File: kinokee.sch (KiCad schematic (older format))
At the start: 14 parts

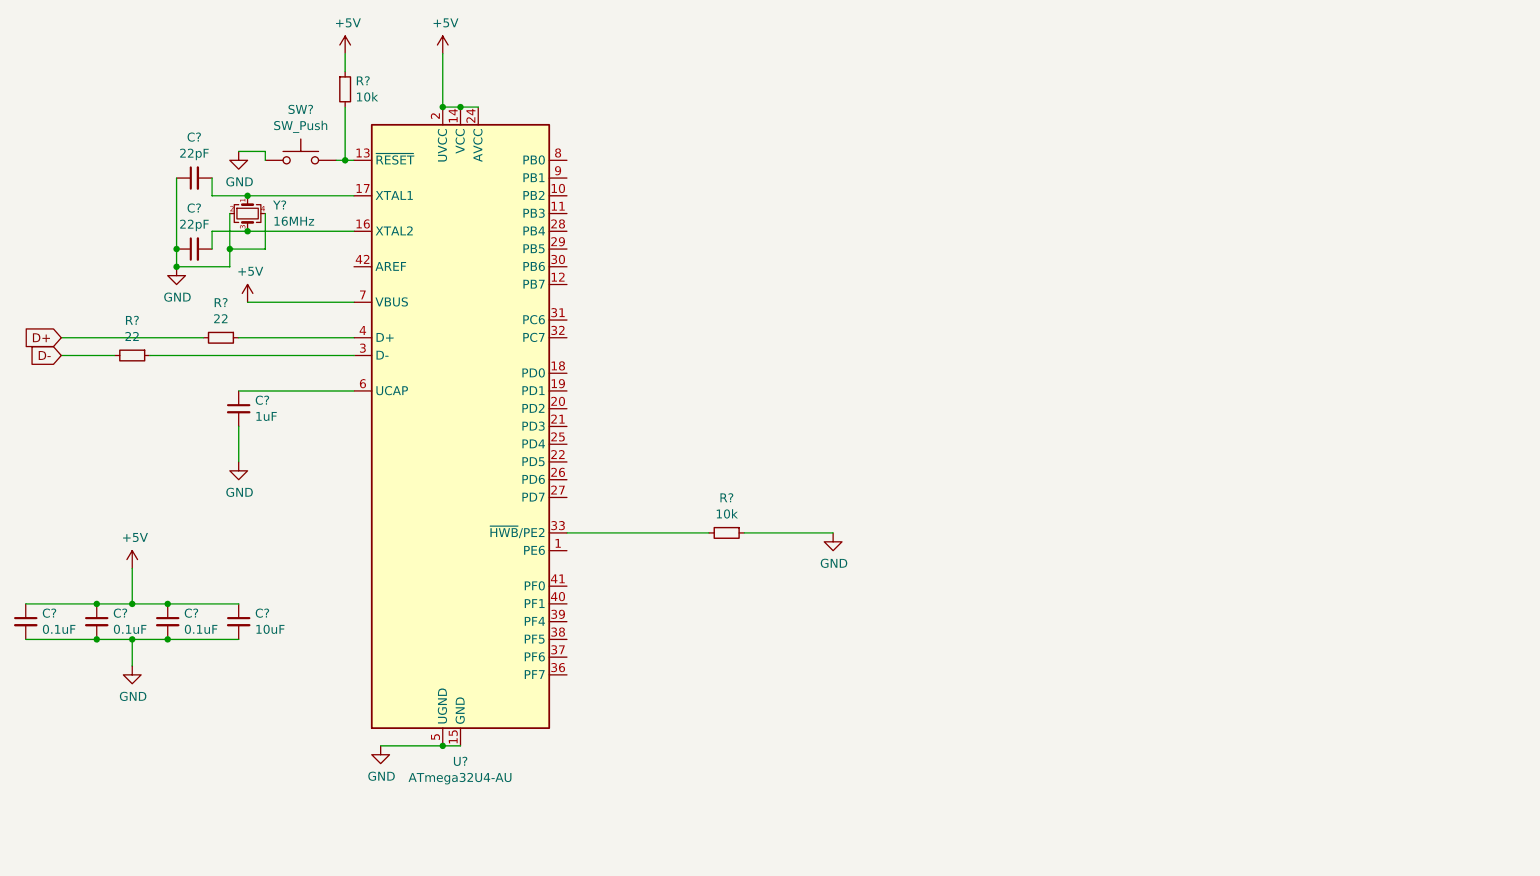
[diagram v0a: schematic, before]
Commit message: add 2x2 matrix and usb to schematic
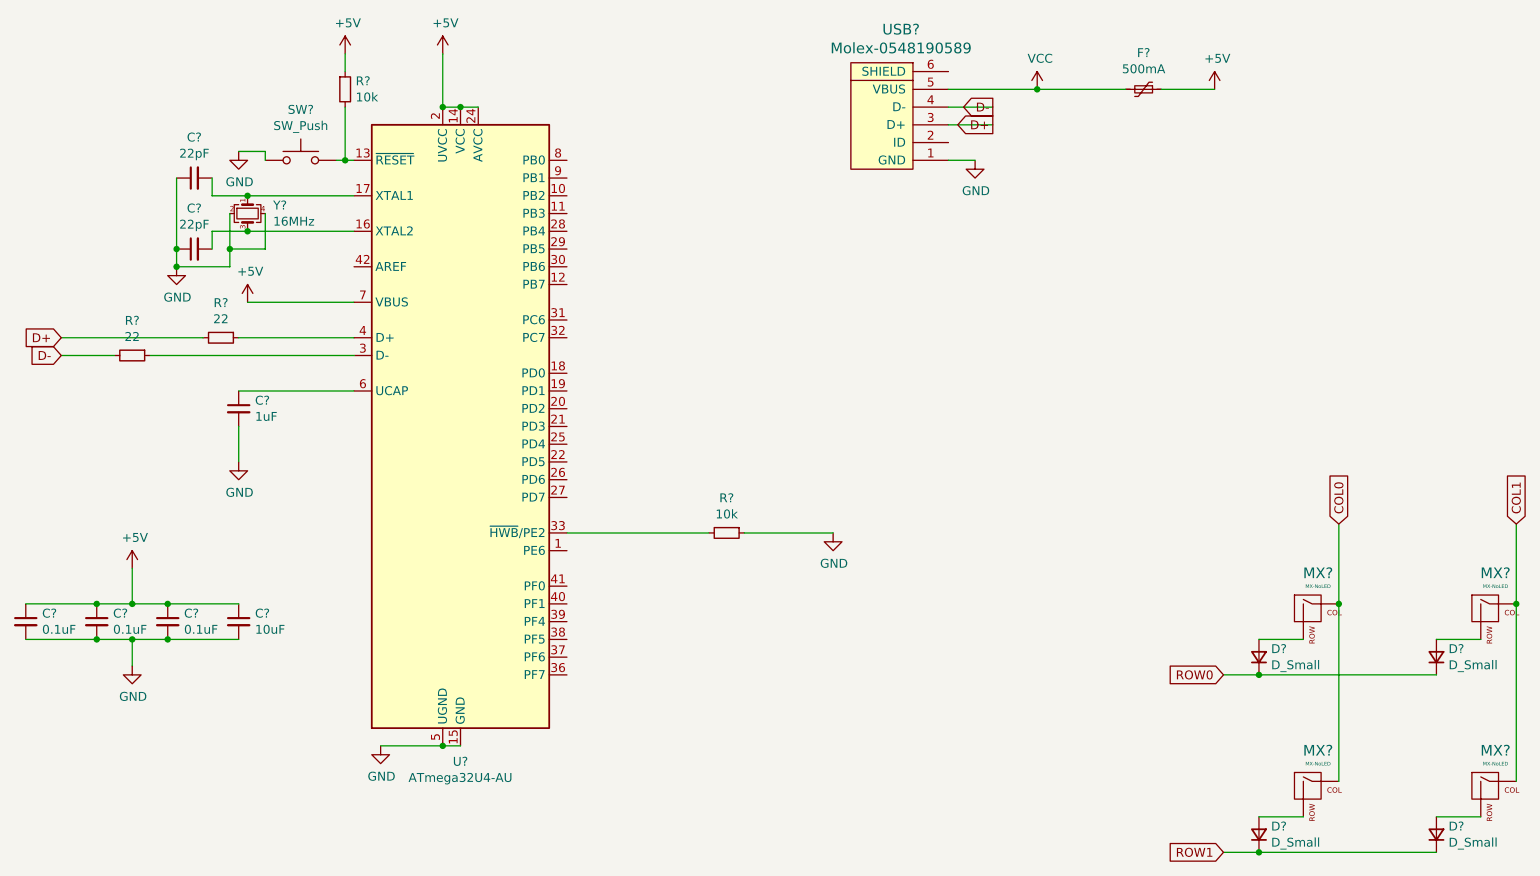
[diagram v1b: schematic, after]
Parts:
- added D? (x4): D_Small, symbol Device:D_Small
- added F?: 500mA, symbol Device:Polyfuse_Small
- added MX? (x4): MX-NoLED, symbol MX_Alps_Hybrid:MX-NoLED
- added USB?: Molex-0548190589, symbol random-keyboard-parts:Molex-0548190589
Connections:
- net +5V: now also F?.1
- net D+: now also USB?.3 (D+)
- net D-: now also USB?.4 (D-)
- net GND: now also USB?.1 (GND)
- new net: D?.2 (A), MX?.2 (ROW) (x4)
- new net COL0: MX?.1 (COL), MX?.1 (COL)
- new net COL1: MX?.1 (COL), MX?.1 (COL)
- new net ROW0: D?.1 (K), D?.1 (K)
- new net ROW1: D?.1 (K), D?.1 (K)
- new net VCC: F?.2, USB?.5 (VBUS)
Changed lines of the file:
@@
 EESchema Schematic File Version 4
+LIBS:kinokee-cache
 EELAYER 30 0
 EELAYER END
@@
 Text GLabel 1500 3100 0    50   Input ~ 0
 D-
+$Comp
+L random-keyboard-parts:Molex-0548190589 USB?
+U 1 1 61B5ADF8
+P 6200 1800
+F 0 "USB?" V 6737 1767 60  0000 C CNN
+F 1 "Molex-0548190589" V 6631 1767 60  0000 C CNN
+F 2 "" H 6200 1800 60  0001 C CNN
+F 3 "" H 6200 1800 60  0001 C CNN
+	1    6200 1800
+	0    -1   -1   0
+$EndComp
+$Comp
+L Device:Polyfuse_Small F?
+U 1 1 61B5F971
+P 7600 1600
+F 0 "F?" V 7395 1600 50  0000 C CNN
+F 1 "500mA" V 7486 1600 50  0000 C CNN
+F 2 "" H 7650 1400 50  0001 L CNN
+F 3 "~" H 7600 1600 50  0001 C CNN
+	1    7600 1600
+	0    1    1    0
+$EndComp
+$Comp
+L power:VCC #PWR?
+U 1 1 61B60F28
+P 7000 1600
+F 0 "#PWR?" H 7000 1450 50  0001 C CNN
+F 1 "VCC" H 7017 1773 50  0000 C CNN
+F 2 "" H 7000 1600 50  0001 C CNN
+F 3 "" H 7000 1600 50  0001 C CNN
+	1    7000 1600
+	1    0    0    -1
+$EndComp
+Wire Wire Line
+	6500 1600 7000 1600
+Wire Wire Line
+	7000 1600 7500 1600
+Connection ~ 7000 1600
+$Comp
+L power:+5V #PWR?
+U 1 1 61B6393F
+P 8000 1600
+F 0 "#PWR?" H 8000 1450 50  0001 C CNN
+F 1 "+5V" H 8015 1773 50  0000 C CNN
+F 2 "" H 8000 1600 50  0001 C CNN
+F 3 "" H 8000 1600 50  0001 C CNN
+	1    8000 1600
+	1    0    0    -1
+$EndComp
+Wire Wire Line
+	7700 1600 8000 1600
+Text GLabel 6750 1800 0    50   Output ~ 0
+D+
+Wire Wire Line
+	6500 1800 6750 1800
+Text GLabel 6750 1700 0    50   Output ~ 0
+D-
+Wire Wire Line
+	6500 1700 6750 1700
+$Comp
+L power:GND #PWR?
+U 1 1 61B68145
+P 6650 2000
+F 0 "#PWR?" H 6650 1750 50  0001 C CNN
+F 1 "GND" H 6655 1827 50  0000 C CNN
+F 2 "" H 6650 2000 50  0001 C CNN
+F 3 "" H 6650 2000 50  0001 C CNN
+	1    6650 2000
+	1    0    0    -1
+$EndComp
+Wire Wire Line
+	6500 2000 6650 2000
+$Comp
+L MX_Alps_Hybrid:MX-NoLED MX?
+U 1 1 61B6983E
+P 8550 4550
+F 0 "MX?" H 8583 4773 60  0000 C CNN
+F 1 "MX-NoLED" H 8583 4699 20  0000 C CNN
+F 2 "" H 7925 4525 60  0001 C CNN
+F 3 "" H 7925 4525 60  0001 C CNN
+	1    8550 4550
+	1    0    0    -1
+$EndComp
+$Comp
+L Device:D_Small D?
+U 1 1 61B6B0B0
+P 8250 4800
+F 0 "D?" V 8296 4732 50  0000 R CNN
+F 1 "D_Small" V 8205 4732 50  0000 R CNN
+F 2 "" V 8250 4800 50  0001 C CNN
+F 3 "~" V 8250 4800 50  0001 C CNN
+	1    8250 4800
+	0    -1   -1   0
+$EndComp
+Wire Wire Line
+	8250 4700 8500 4700
+$Comp
+L MX_Alps_Hybrid:MX-NoLED MX?
+U 1 1 61B6D2F5
+P 9550 4550
+F 0 "MX?" H 9583 4773 60  0000 C CNN
+F 1 "MX-NoLED" H 9583 4699 20  0000 C CNN
+F 2 "" H 8925 4525 60  0001 C CNN
+F 3 "" H 8925 4525 60  0001 C CNN
+	1    9550 4550
+	1    0    0    -1
+$EndComp
+$Comp
+L Device:D_Small D?
+U 1 1 61B6E845
+P 9250 4800
+F 0 "D?" V 9296 4732 50  0000 R CNN
+F 1 "D_Small" V 9205 4732 50  0000 R CNN
+F 2 "" V 9250 4800 50  0001 C CNN
+F 3 "~" V 9250 4800 50  0001 C CNN
+	1    9250 4800
+	0    -1   -1   0
+$EndComp
+$Comp
+L MX_Alps_Hybrid:MX-NoLED MX?
+U 1 1 61B7046B
+P 8550 5550
+F 0 "MX?" H 8583 5773 60  0000 C CNN
+F 1 "MX-NoLED" H 8583 5699 20  0000 C CNN
+F 2 "" H 7925 5525 60  0001 C CNN
+F 3 "" H 7925 5525 60  0001 C CNN
+	1    8550 5550
+	1    0    0    -1
+$EndComp
+$Comp
+L Device:D_Small D?
+U 1 1 61B70F93
+P 8250 5800
+F 0 "D?" V 8296 5732 50  0000 R CNN
+F 1 "D_Small" V 8205 5732 50  0000 R CNN
+F 2 "" V 8250 5800 50  0001 C CNN
+F 3 "~" V 8250 5800 50  0001 C CNN
+	1    8250 5800
+	0    -1   -1   0
+$EndComp
+$Comp
+L Device:D_Small D?
+U 1 1 61B71E0D
+P 9250 5800
+F 0 "D?" V 9296 5732 50  0000 R CNN
+F 1 "D_Small" V 9205 5732 50  0000 R CNN
+F 2 "" V 9250 5800 50  0001 C CNN
+F 3 "~" V 9250 5800 50  0001 C CNN
+	1    9250 5800
+	0    -1   -1   0
+$EndComp
+$Comp
+L MX_Alps_Hybrid:MX-NoLED MX?
+U 1 1 61B731E6
+P 9550 5550
+F 0 "MX?" H 9583 5773 60  0000 C CNN
+F 1 "MX-NoLED" H 9583 5699 20  0000 C CNN
+F 2 "" H 8925 5525 60  0001 C CNN
+F 3 "" H 8925 5525 60  0001 C CNN
+	1    9550 5550
+	1    0    0    -1
+$EndComp
+Wire Wire Line
+	8250 5700 8500 5700
+Wire Wire Line
+	9250 5700 9500 5700
+Wire Wire Line
+	9250 4700 9500 4700
+Wire Wire Line
+	8250 4900 9250 4900
+Wire Wire Line
+	8700 4500 8700 4050
+Wire Wire Line
+	9700 4500 9700 4050
+Wire Wire Line
+	9700 5500 9700 4500
+Connection ~ 9700 4500
+Wire Wire Line
+	9250 5900 8250 5900
+Wire Wire Line
+	8250 5900 8050 5900
+Connection ~ 8250 5900
+Wire Wire Line
+	8250 4900 8050 4900
+Connection ~ 8250 4900
+Wire Wire Line
+	8700 5500 8700 4500
+Connection ~ 8700 4500
+Text GLabel 8050 4900 0    50   Input ~ 0
+ROW0
+Text GLabel 8050 5900 0    50   Input ~ 0
+ROW1
+Text GLabel 8700 4050 1    50   Input ~ 0
+COL0
+Text GLabel 9700 4050 1    50   Input ~ 0
+COL1
 $EndSCHEMATC

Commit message: assign footprints to schematic
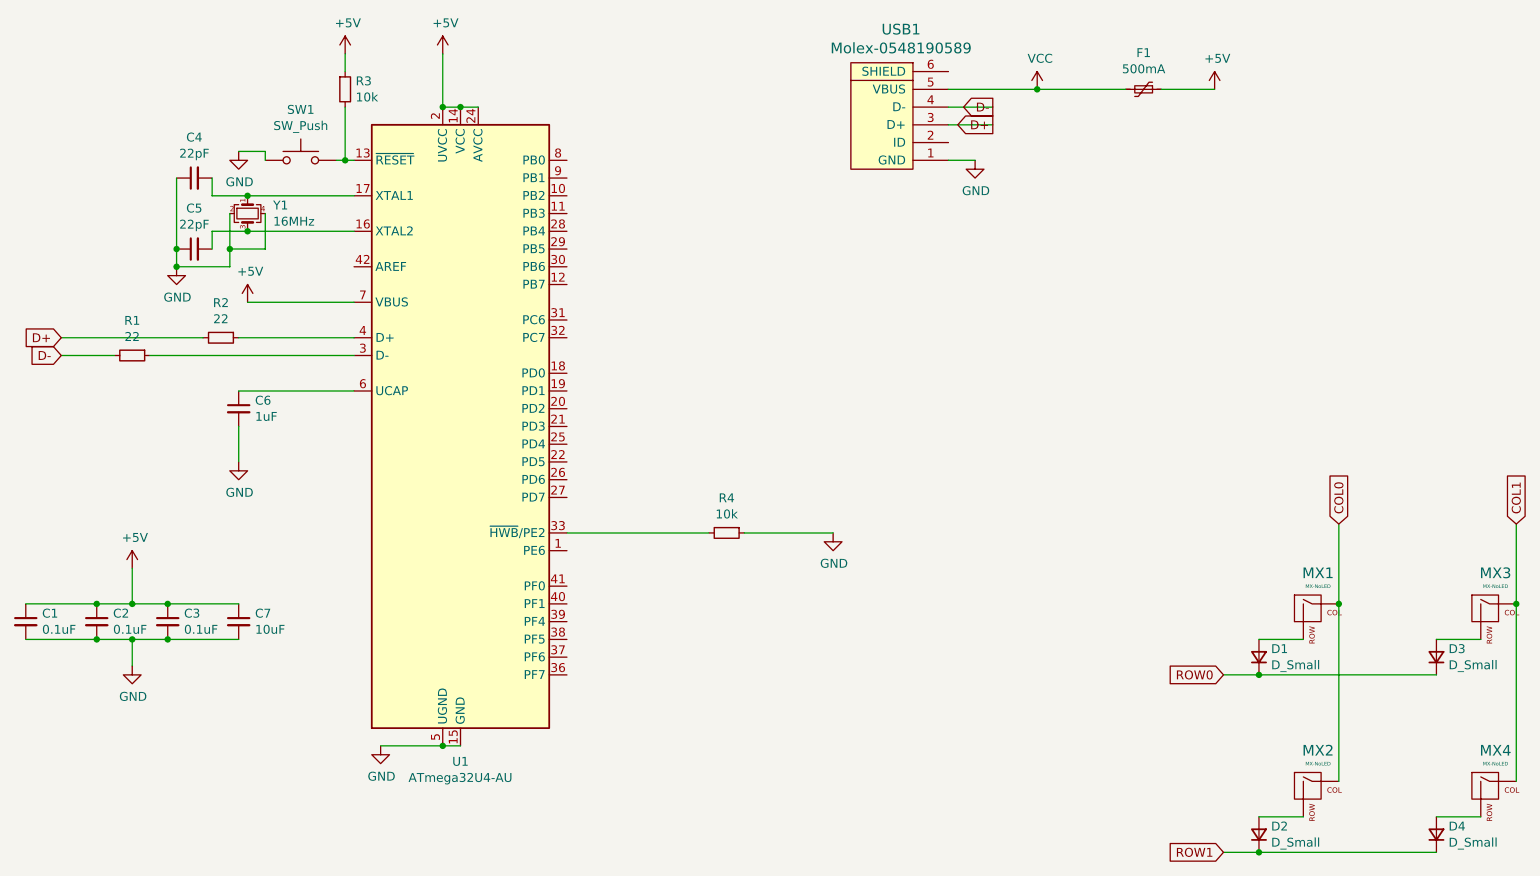
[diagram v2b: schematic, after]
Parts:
- C1, C2, C3, C4, C5, C6, C7: renamed from C?; footprint (none) -> Capacitor_THT:C_Rect_L41.5mm_W35.0mm_P37.50mm_MKS4
- D1, D2, D3, D4: renamed from D?; footprint (none) -> Diode_SMD:D_SOD-123
- F1: renamed from F?; footprint (none) -> Fuse:Fuse_1206_3216Metric
- MX1, MX2, MX3, MX4: renamed from MX?; footprint (none) -> MX_Alps_Hybrid:MX-1U-NoLED
- R1, R2, R3, R4: renamed from R?; footprint (none) -> Resistor_SMD:R_0805_2012Metric
- SW1: renamed from SW?; footprint (none) -> random-keyboard-parts:SKQG-1155865
- USB1: renamed from USB?; footprint (none) -> random-keyboard-parts:Molex-0548190589
- Y1: renamed from Y?; footprint (none) -> Crystal:Crystal_SMD_3225-4Pin_3.2x2.5mm
- gave numbers to parts that had none: 1

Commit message: fix capacitor footprint
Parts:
- C1, C2, C3, C4, C5, C6, C7: footprint Capacitor_THT:C_Rect_L41.5mm_W35.0mm_P37.50mm_MKS4 -> Capacitor_SMD:C_0805_2012Metric
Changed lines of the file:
@@
 EESchema Schematic File Version 4
-LIBS:kinokee-cache
 EELAYER 30 0
 EELAYER END
@@
 F 0 "C6" H 2592 3446 50  0000 L CNN
 F 1 "1uF" H 2592 3355 50  0000 L CNN
-F 2 "Capacitor_THT:C_Rect_L41.5mm_W35.0mm_P37.50mm_MKS4" H 2500 3400 50  0001 C CNN
+F 2 "Capacitor_SMD:C_0805_2012Metric" H 2500 3400 50  0001 C CNN
 F 3 "~" H 2500 3400 50  0001 C CNN
 	1    2500 3400
@@
 F 0 "C1" H 1392 4646 50  0000 L CNN
 F 1 "0.1uF" H 1392 4555 50  0000 L CNN
-F 2 "Capacitor_THT:C_Rect_L41.5mm_W35.0mm_P37.50mm_MKS4" H 1300 4600 50  0001 C CNN
+F 2 "Capacitor_SMD:C_0805_2012Metric" H 1300 4600 50  0001 C CNN
 F 3 "~" H 1300 4600 50  0001 C CNN
 	1    1300 4600
@@
 F 0 "C2" H 1792 4646 50  0000 L CNN
 F 1 "0.1uF" H 1792 4555 50  0000 L CNN
-F 2 "Capacitor_THT:C_Rect_L41.5mm_W35.0mm_P37.50mm_MKS4" H 1700 4600 50  0001 C CNN
+F 2 "Capacitor_SMD:C_0805_2012Metric" H 1700 4600 50  0001 C CNN
 F 3 "~" H 1700 4600 50  0001 C CNN
 	1    1700 4600
@@
 F 0 "C3" H 2192 4646 50  0000 L CNN
 F 1 "0.1uF" H 2192 4555 50  0000 L CNN
-F 2 "Capacitor_THT:C_Rect_L41.5mm_W35.0mm_P37.50mm_MKS4" H 2100 4600 50  0001 C CNN
+F 2 "Capacitor_SMD:C_0805_2012Metric" H 2100 4600 50  0001 C CNN
 F 3 "~" H 2100 4600 50  0001 C CNN
 	1    2100 4600
@@
 F 0 "C7" H 2592 4646 50  0000 L CNN
 F 1 "10uF" H 2592 4555 50  0000 L CNN
-F 2 "Capacitor_THT:C_Rect_L41.5mm_W35.0mm_P37.50mm_MKS4" H 2500 4600 50  0001 C CNN
+F 2 "Capacitor_SMD:C_0805_2012Metric" H 2500 4600 50  0001 C CNN
 F 3 "~" H 2500 4600 50  0001 C CNN
 	1    2500 4600
@@
 F 0 "C4" V 2479 2100 50  0000 C CNN
 F 1 "22pF" V 2388 2100 50  0000 C CNN
-F 2 "Capacitor_THT:C_Rect_L41.5mm_W35.0mm_P37.50mm_MKS4" H 2250 2100 50  0001 C CNN
+F 2 "Capacitor_SMD:C_0805_2012Metric" H 2250 2100 50  0001 C CNN
 F 3 "~" H 2250 2100 50  0001 C CNN
 	1    2250 2100
@@
 F 0 "C5" V 2479 2500 50  0000 C CNN
 F 1 "22pF" V 2388 2500 50  0000 C CNN
-F 2 "Capacitor_THT:C_Rect_L41.5mm_W35.0mm_P37.50mm_MKS4" H 2250 2500 50  0001 C CNN
+F 2 "Capacitor_SMD:C_0805_2012Metric" H 2250 2500 50  0001 C CNN
 F 3 "~" H 2250 2500 50  0001 C CNN
 	1    2250 2500

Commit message: sketch component placement
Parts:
- renumbered MX3 to MX2, MX2 to MX3
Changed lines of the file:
@@
 	8250 4700 8500 4700
 $Comp
-L MX_Alps_Hybrid:MX-NoLED MX3
+L MX_Alps_Hybrid:MX-NoLED MX2
 U 1 1 61B6D2F5
 P 9550 4550
-F 0 "MX3" H 9583 4773 60  0000 C CNN
+F 0 "MX2" H 9583 4773 60  0000 C CNN
 F 1 "MX-NoLED" H 9583 4699 20  0000 C CNN
 F 2 "MX_Alps_Hybrid:MX-1U-NoLED" H 8925 4525 60  0001 C CNN
@@
 $EndComp
 $Comp
-L MX_Alps_Hybrid:MX-NoLED MX2
+L MX_Alps_Hybrid:MX-NoLED MX3
 U 1 1 61B7046B
 P 8550 5550
-F 0 "MX2" H 8583 5773 60  0000 C CNN
+F 0 "MX3" H 8583 5773 60  0000 C CNN
 F 1 "MX-NoLED" H 8583 5699 20  0000 C CNN
 F 2 "MX_Alps_Hybrid:MX-1U-NoLED" H 7925 5525 60  0001 C CNN
